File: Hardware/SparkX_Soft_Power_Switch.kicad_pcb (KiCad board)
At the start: 2 copper layers, 25.4 x 25.4 mm, 62 parts, among them J1 JST_2mm_LiPo, J2 JST_2mm_LiPo, J3 Conn_01x06, Q1 BSS138, Q2 BSS138, SW1 SMD_5.2x5.2mm_h1.9mm, U2 74LVC1G14, U3 74LVC1G17, U4 74LVC1G175, U5 MIC94064YC6

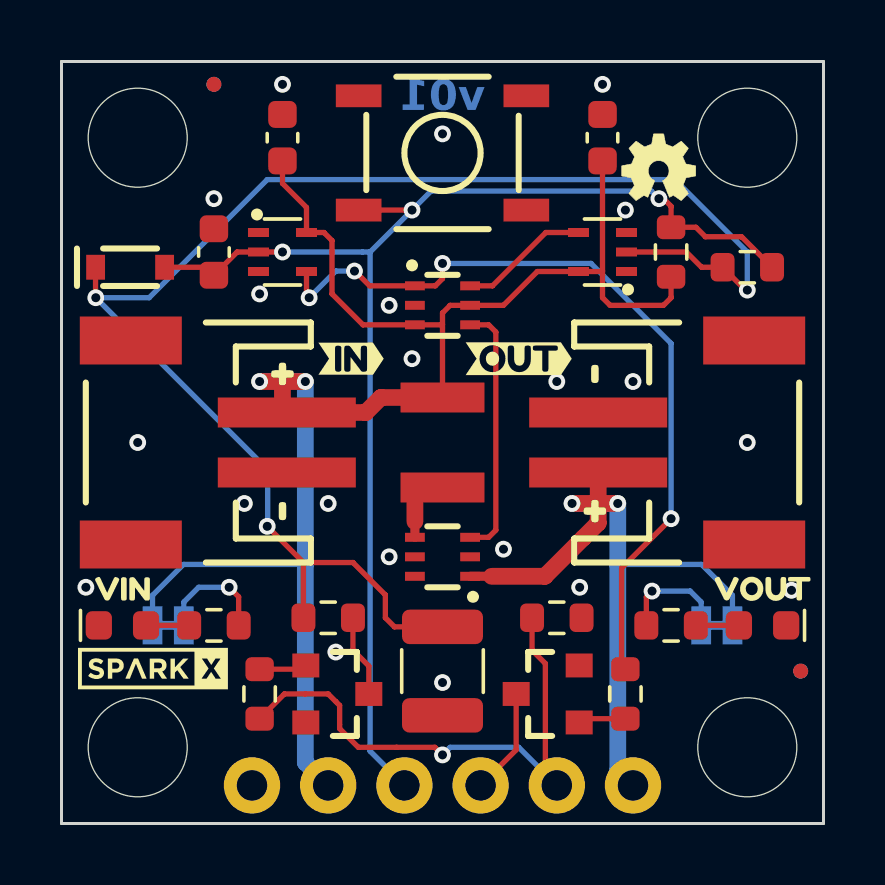
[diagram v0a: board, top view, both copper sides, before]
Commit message: Change to SIL2308 - for battery charging
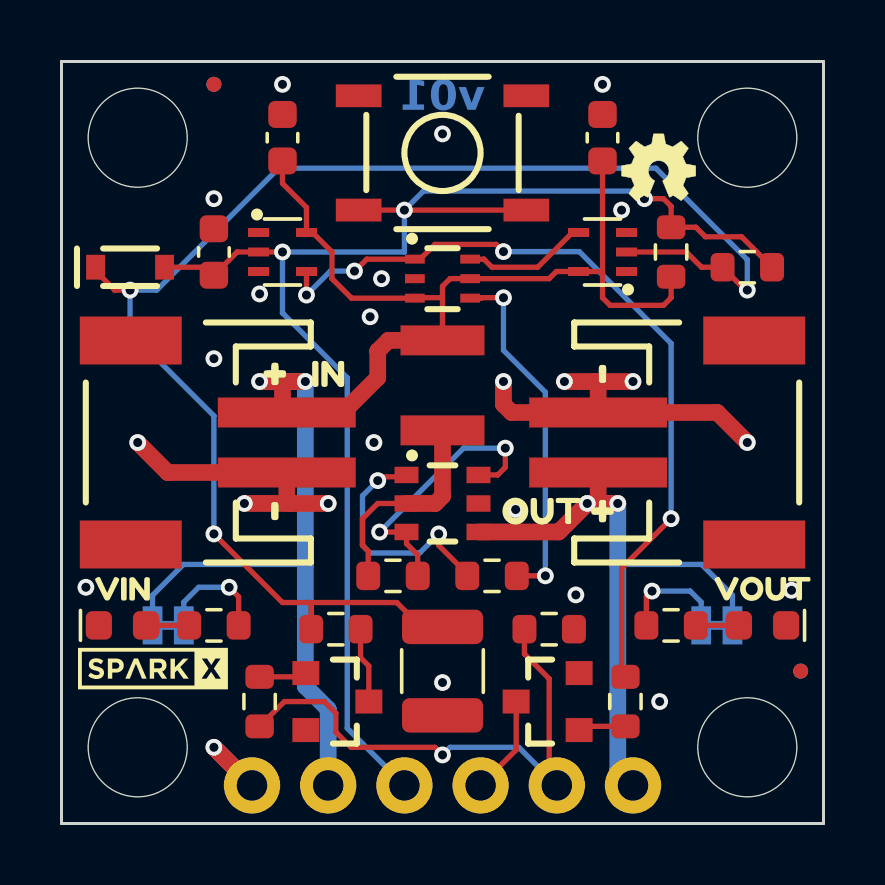
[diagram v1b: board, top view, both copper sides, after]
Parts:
- removed U1: ~, SparkFun-Aesthetic:Ordering_Instructions
- removed U5: MIC94064YC6, SparkFun-Semiconductor-Standard:SOT-323
- removed kibuzzard-65F05285: G***, kibuzzard-65F05285
- removed kibuzzard-65F052A4: G***, kibuzzard-65F052A4
- added Q3: SIL2308, SparkFun-Semiconductor-Standard:SOT23-6-Tight, F.Cu at (128.3, 113.8)
- added R10: 100k, SparkFun-Resistor:R_0603_1608Metric, F.Cu at (126.6, 116.2)
- added R9: 1k, SparkFun-Resistor:R_0603_1608Metric, F.Cu at (129.9, 116.2)
- added kibuzzard-65F174FD: G***, kibuzzard-65F174FD, F.Cu at (131.6, 114.0)
- added kibuzzard-65F1758C: G***, kibuzzard-65F1758C, F.Cu at (124.5, 109.5)
- R6, R8: value 100 -> 1k
- moved G3 9.65 mm to (212.1, 168.1)
- moved F1 1.91 mm to (128.3, 109.9)
- moved U4 0.89 mm to (128.3, 106.3)
- moved R7 0.46 mm to (131.8, 118.0)
- moved R5 0.46 mm to (124.7, 118.0)
- moved G*** 0.38 mm to (128.3, 103.1)
- moved kibuzzard-65F04F60 0.25 mm to (133.6, 114.0)
- moved kibuzzard-65F04FCA 0.25 mm to (133.6, 109.5)
- moved Q1 0.25 mm to (124.7, 120.4)
- moved Q2 0.25 mm to (131.8, 120.4)
- moved R6 0.25 mm to (122.2, 120.4)
- moved R8 0.25 mm to (134.4, 120.4)
- moved kibuzzard-65F04F60 0.25 mm to (122.7, 109.5)
- moved kibuzzard-65F04FCA 0.25 mm to (122.7, 114.0)
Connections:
- net Off renamed OFF
- net Push renamed PUSH
- C1 pad 1: Button -> BTN
- D1 pad A: Button -> BTN
- J3 pad 4: Button -> BTN
- R1 pad 2: Button -> BTN
- R2 pad 2: Button -> BTN
- SW1 pad 2: (no net) -> BTN
- U2 pad 2: Button -> BTN
- U4 pad 4: Net-(U4-Q) -> EN
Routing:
- net BTN: track 0.00 -> 48.9 mm, vias 0 -> 3
- net Button: track 43.0 -> 0.00 mm, vias 3 -> 0
- net GND: track 0.00 -> 25.6 mm, vias 21 -> 24
- net EN: track 0.00 -> 11.9 mm, vias 0 -> 2
- net Net-(Q3A-D): track 0.00 -> 9.50 mm, vias 0 -> 2
- net Net-(U4-Q): track 8.52 -> 0.00 mm
- net Net-(Q3A-G): track 0.00 -> 8.11 mm, vias 0 -> 2
- net Net-(Q3B-1): track 3.35 -> 7.16 mm
- net VOUT: track 24.6 -> 21.9 mm
- net VIN: track 55.9 -> 54.9 mm
- net Net-(C2-Pad1): track 50.7 -> 49.8 mm

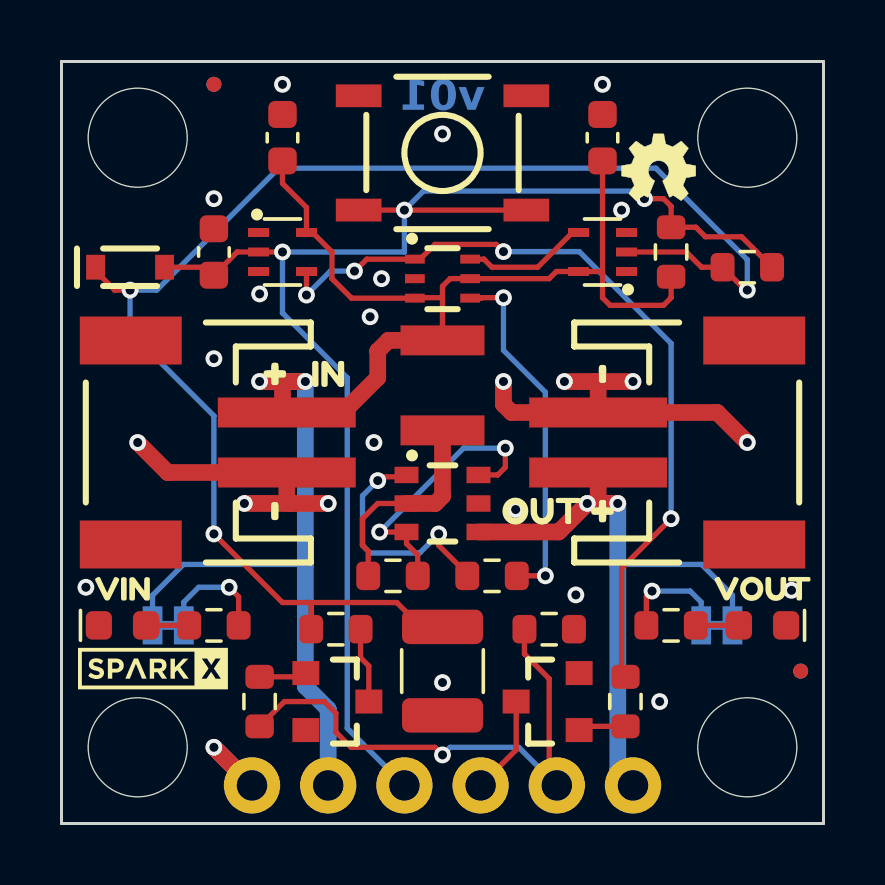
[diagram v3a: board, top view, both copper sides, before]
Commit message: Update to KiCad 8. Update 47uF cap
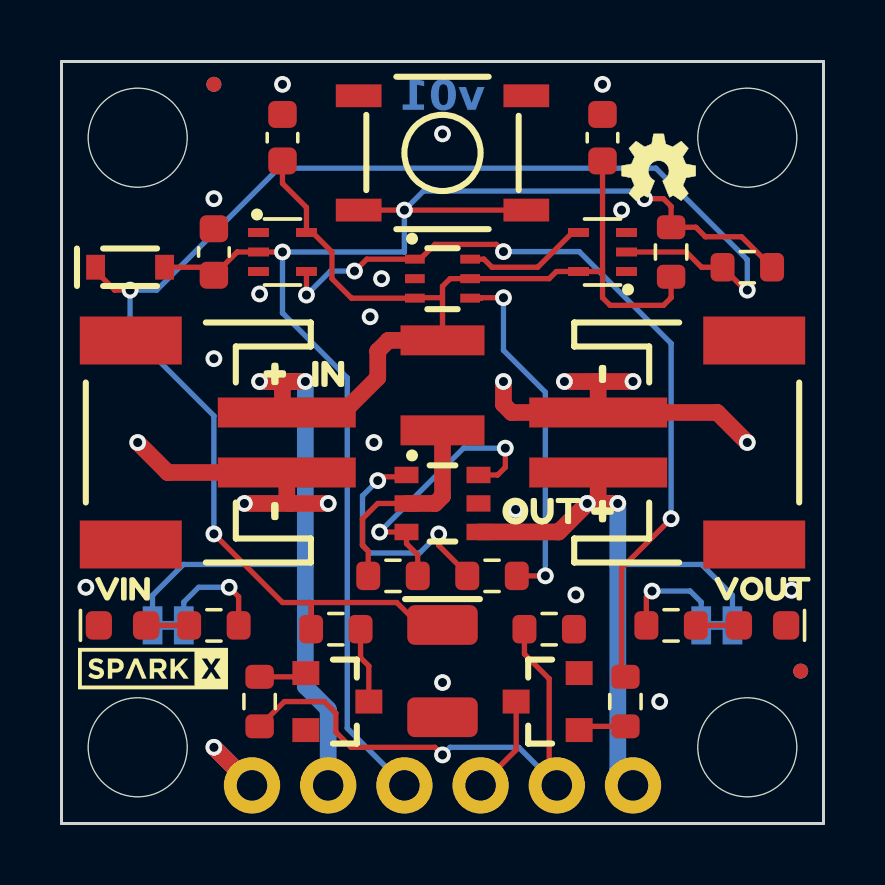
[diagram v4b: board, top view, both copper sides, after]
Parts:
- removed kibuzzard-65F056B4: G***, kibuzzard-65F056B4
- C2: footprint SparkFun-Capacitor:C_1210_3225Metric -> SparkFun-Capacitor:EIA-3528

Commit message: Update 3D models
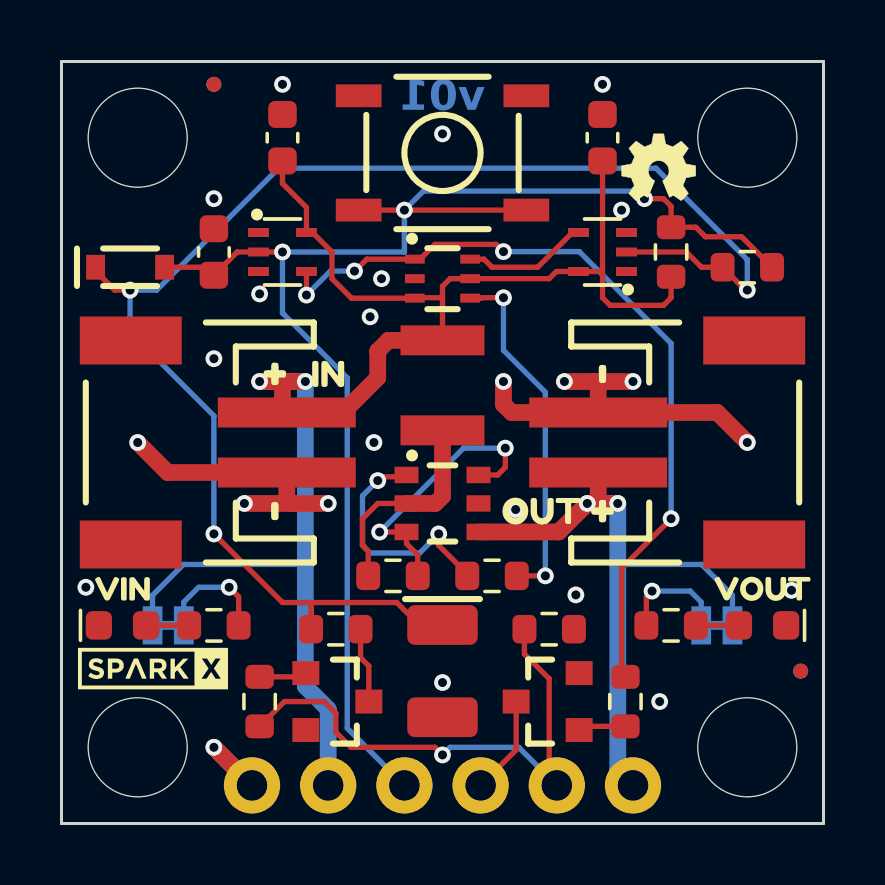
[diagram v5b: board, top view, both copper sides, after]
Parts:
- D2, D3: footprint SparkFun-LED:LED_0603_1608Metric -> SparkFun-LED:LED_0603_1608Metric_Red
- SW1: footprint SparkFun-Switch:Push_SMD_5.2x5.2mm -> SparkFun-Switch:Push_SMD_5.2x5.2mm_h1.9mm
